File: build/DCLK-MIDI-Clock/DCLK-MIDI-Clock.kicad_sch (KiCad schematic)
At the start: 24 parts, among them J1 MIDI OUT, J2 Jack-DC, J3 MIDI OUT, SW1 CH1, SW2 CH2, SW3 SETTINGS, SW4 RotaryEncoder_Switch_MP

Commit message: pcb rev2
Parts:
- removed F1: 1A_15V, Fuse:Fuse_1812_4532Metric, symbol PCM_4ms_Regulator:Polyfuse_3A_15V
- removed SW1: CH1, Button_Switch_Keyboard:SW_Cherry_MX_1.00u_PCB, symbol Switch:SW_SPST
- removed SW2: CH2, Button_Switch_Keyboard:SW_Cherry_MX_1.00u_PCB, symbol Switch:SW_SPST
- removed SW3: SETTINGS, Button_Switch_Keyboard:SW_Cherry_MX_1.00u_PCB, symbol Switch:SW_SPST
- added C7, C8, C9: 10nF, Capacitor_SMD:C_1206_3216Metric_Pad1.33x1.80mm_HandSolder, symbol Device:C
- added J4: MIDI OUT, audioConnectors_Edit:Jack_3.5mm_CUI_SJ1-3525N_Horizontal_edit, symbol Connector_Audio:AudioJack3
- added J5: Conn_02x04_Odd_Even, Connector_PinSocket_2.54mm:PinSocket_2x04_P2.54mm_Vertical, symbol Connector_Generic:Conn_02x04_Odd_Even
- added J6: Conn_02x04_Odd_Even, Connector_PinHeader_2.54mm:PinHeader_2x04_P2.54mm_Vertical_SMD, symbol Connector_Generic:Conn_02x04_Odd_Even
- added R10: 10k, PCM_4ms_Resistor:R_0603, symbol PCM_4ms_Resistor:10k_0402
- added R5, R6: 4k7, PCM_4ms_Resistor:R_0603, symbol PCM_4ms_Resistor:10k_0402
- added R7, R8, R9: 330R, PCM_4ms_Resistor:R_0603, symbol PCM_4ms_Resistor:10k_0402
- added U2: CAP1206-x-SL, Package_SO:SOIC-14_3.9x8.7mm_P1.27mm, symbol Sensor_Touch:CAP1206-x-SL
- SSD1306: footprint SSD1306_footprint:SSD1306_OLED_Module -> SSD1306:SSD1306-128x32
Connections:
- net 3V3: now also C9.2, R10.2, R5.1, R6.1, U2.7 (VDD)
- net A: now also U1.12 (PB4/SCL2), C7.1
- net B: now also U1.13 (PB5), C8.1
- net CH1: now also J5.1 (Pin_1), J5.2 (Pin_2), J6.1 (Pin_1), J6.2 (Pin_2), U2.2 (CS1); no longer U1.34 (PB0/ADC8)
- net CH2: now also J5.3 (Pin_3), J5.4 (Pin_4), J6.3 (Pin_3), J6.4 (Pin_4), U2.13 (CS2); no longer U1.35 (PB1/ADC9)
- net ENCODER: now also U1.2 (PB13/SCK4)
- net GND: now also C7.2, C8.2, C9.1, U2.10 (CS5), U2.11 (CS4), U2.8 (GND), U2.9 (CS6)
- net LED_BEAT: now also R9.1; no longer D4.2
- net LED_CH1: now also R7.1; no longer D2.2
- net LED_CH2: now also R8.1; no longer D3.2
- net SCL0: now also R5.2, U2.5 (SMCLK)
- net SDA0: now also R6.2, U2.4 (SMDATA)
- net SETTINGS: now also J5.5 (Pin_5), J5.6 (Pin_6), J6.5 (Pin_5), J6.6 (Pin_6), U2.12 (CS3)
- net TX0: now also U1.6 (PA9/TX1); no longer U1.28 (PA2/ADC2/TX2)
- net TX1: now also U1.28 (PA2/ADC2/TX2); no longer U1.6 (PA9/TX1)
- net ISR: now reaches U1.1 (PB12/SCK3)
- net ISR: now also R10.1, U2.3 (ALERT#)
- net at C1.2, C2.1, D1.2 (A): now also J2.1
- new net: D3.2, R8.2
- new net: D4.2, R9.2
- new net: D2.2, R7.2
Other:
- note added: "5V ONLY DC Input"
- note added: "ENCODER"
- note added: "SYNC IN"
- note added: "TOUCH BUTTONS"
- note removed: "5V DC Input"
- note removed: "BUTTONS & ENCODER"
- moved on the sheet: C1, C2, C6, D1, D2, D3, D4, SSD1306, SW4

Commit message: pcb rev2
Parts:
- removed J4: MIDI OUT, audioConnectors_Edit:Jack_3.5mm_CUI_SJ1-3525N_Horizontal_edit, symbol Connector_Audio:AudioJack3
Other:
- note removed: "SYNC IN"
- moved on the sheet: J5, J6
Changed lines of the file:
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@@
 	)
 	(rectangle
-		(start 13.97 125.73)
-		(end 57.15 163.83)
-		(stroke
-			(width 0)
-			(type default)
-		)
-		(fill
-			(type none)
-		)
-	)
-	(rectangle
 		(start 102.87 86.36)
 		(end 146.05 124.46)
@@
 		)
 	)
-	(text "SYNC IN"
-		(exclude_from_sim no)
-		(at 14.732 127.762 0)
-		(effects
-			(font
-				(face "Alagard")
-				(size 2.54 2.54)
-			)
-			(justify left)
-		)
-	)
 	(text "MIDI CH2\n"
 		(exclude_from_sim no)
@@
 	(global_label "SETTINGS"
 		(shape input)
-		(at 67.31 151.13 270)
+		(at 24.13 149.86 270)
 		(fields_autoplaced yes)
 		(effects
@@
 		)
 		(property "Intersheetrefs" "${INTERSHEET_REFS}"
-			(at 67.31 162.8237 90)
+			(at 24.13 161.5537 90)
 			(effects
 				(font
@@
 	(global_label "SETTINGS"
 		(shape input)
-		(at 83.82 151.13 270)
+		(at 40.64 149.86 270)
 		(fields_autoplaced yes)
 		(effects
@@
 		)
 		(property "Intersheetrefs" "${INTERSHEET_REFS}"
-			(at 83.82 162.8237 90)
+			(at 40.64 161.5537 90)
 			(effects
 				(font
@@
 	(global_label "CH2"
 		(shape input)
-		(at 81.28 138.43 90)
+		(at 38.1 137.16 90)
 		(fields_autoplaced yes)
 		(effects
@@
 		)
 		(property "Intersheetrefs" "${INTERSHEET_REFS}"
-			(at 81.28 131.6348 90)
+			(at 38.1 130.3648 90)
 			(effects
 				(font
@@
 	(global_label "CH2"
 		(shape input)
-		(at 64.77 151.13 270)
+		(at 21.59 149.86 270)
 		(fields_autoplaced yes)
 		(effects
@@
 		)
 		(property "Intersheetrefs" "${INTERSHEET_REFS}"
-			(at 64.77 157.9252 90)
+			(at 21.59 156.6552 90)
 			(effects
 				(font
@@
 	(global_label "CH2"
 		(shape input)
-		(at 81.28 151.13 270)
+		(at 38.1 149.86 270)
 		(fields_autoplaced yes)
 		(effects
@@
 		)
 		(property "Intersheetrefs" "${INTERSHEET_REFS}"
-			(at 81.28 157.9252 90)
+			(at 38.1 156.6552 90)
 			(effects
 				(font
@@
 	(global_label "CH1"
 		(shape input)
-		(at 62.23 151.13 270)
+		(at 19.05 149.86 270)
 		(fields_autoplaced yes)
 		(effects
@@
 		)
 		(property "Intersheetrefs" "${INTERSHEET_REFS}"
-			(at 62.23 157.9252 90)
+			(at 19.05 156.6552 90)
 			(effects
 				(font
@@
 	(global_label "SETTINGS"
 		(shape input)
-		(at 67.31 138.43 90)
+		(at 24.13 137.16 90)
 		(fields_autoplaced yes)
 		(effects
@@
 		)
 		(property "Intersheetrefs" "${INTERSHEET_REFS}"
-			(at 67.31 126.7363 90)
+			(at 24.13 125.4663 90)
 			(effects
 				(font
@@
 	(global_label "CH1"
 		(shape input)
-		(at 78.74 138.43 90)
+		(at 35.56 137.16 90)
 		(fields_autoplaced yes)
 		(effects
@@
 		)
 		(property "Intersheetrefs" "${INTERSHEET_REFS}"
-			(at 78.74 131.6348 90)
+			(at 35.56 130.3648 90)
 			(effects
 				(font
@@
 	(global_label "CH1"
 		(shape input)
-		(at 62.23 138.43 90)
+		(at 19.05 137.16 90)
 		(fields_autoplaced yes)
 		(effects
@@
 		)
 		(property "Intersheetrefs" "${INTERSHEET_REFS}"
-			(at 62.23 131.6348 90)
+			(at 19.05 130.3648 90)
 			(effects
 				(font
@@
 	(global_label "CH1"
 		(shape input)
-		(at 78.74 151.13 270)
+		(at 35.56 149.86 270)
 		(fields_autoplaced yes)
 		(effects
@@
 		)
 		(property "Intersheetrefs" "${INTERSHEET_REFS}"
-			(at 78.74 157.9252 90)
+			(at 35.56 156.6552 90)
 			(effects
 				(font
@@
 	(global_label "SETTINGS"
 		(shape input)
-		(at 83.82 138.43 90)
+		(at 40.64 137.16 90)
 		(fields_autoplaced yes)
 		(effects
@@
 		)
 		(property "Intersheetrefs" "${INTERSHEET_REFS}"
-			(at 83.82 126.7363 90)
+			(at 40.64 125.4663 90)
 			(effects
 				(font
@@
 	(global_label "CH2"
 		(shape input)
-		(at 64.77 138.43 90)
+		(at 21.59 137.16 90)
 		(fields_autoplaced yes)
 		(effects
@@
 		)
 		(property "Intersheetrefs" "${INTERSHEET_REFS}"
-			(at 64.77 131.6348 90)
+			(at 21.59 130.3648 90)
 			(effects
 				(font
@@
 	(symbol
 		(lib_id "Connector_Generic:Conn_02x04_Odd_Even")
-		(at 64.77 146.05 90)
+		(at 21.59 144.78 90)
 		(unit 1)
 		(exclude_from_sim no)
@@
 		(fields_autoplaced yes)
 		(property "Reference" "J5"
-			(at 72.39 143.5099 90)
+			(at 29.21 142.2399 90)
 			(effects
 				(font
@@
 		)
 		(property "Value" "Conn_02x04_Odd_Even"
-			(at 72.39 146.0499 90)
+			(at 29.21 144.7799 90)
 			(effects
 				(font
@@
 		)
 		(property "Footprint" "Connector_PinSocket_2.54mm:PinSocket_2x04_P2.54mm_Vertical"
-			(at 64.77 146.05 0)
+			(at 21.59 144.78 0)
 			(effects
 				(font
@@
 		)
 		(property "Datasheet" "~"
-			(at 64.77 146.05 0)
+			(at 21.59 144.78 0)
 			(effects
 				(font
@@
 		)
 		(property "Description" "Generic connector, double row, 02x04, odd/even pin numbering scheme (row 1 odd numbers, row 2 even numbers), script generated (kicad-library-utils/schlib/autogen/connector/)"
-			(at 64.77 146.05 0)
+			(at 21.59 144.78 0)
 			(effects
 				(font
@@
 	)
 	(symbol
-		(lib_id "Connector_Audio:AudioJack3")
-		(at 21.59 139.7 0)
-		(unit 1)
-		(exclude_from_sim no)
-		(in_bom yes)
-		(on_board yes)
-		(dnp no)
-		(fields_autoplaced yes)
-		(property "Reference" "J4"
-			(at 19.685 130.81 0)
-			(effects
-				(font
-					(size 1.27 1.27)
-				)
-			)
-		)
-		(property "Value" "MIDI OUT"
-			(at 19.685 133.35 0)
-			(effects
-				(font
-					(size 1.27 1.27)
-				)
-			)
-		)
-		(property "Footprint" "audioConnectors_Edit:Jack_3.5mm_CUI_SJ1-3525N_Horizontal_edit"
-			(at 21.59 139.7 0)
-			(effects
-				(font
-					(size 1.27 1.27)
-				)
-				(hide yes)
-			)
-		)
-		(property "Datasheet" "~"
-			(at 21.59 139.7 0)
-			(effects
-				(font
-					(size 1.27 1.27)
-				)
-				(hide yes)
-			)
-		)
-		(property "Description" "Audio Jack, 3 Poles (Stereo / TRS)"
-			(at 21.59 139.7 0)
-			(effects
-				(font
-					(size 1.27 1.27)
-				)
-				(hide yes)
-			)
-		)
-		(pin "S"
-		)
-		(pin "T"
-		)
-		(pin "R"
-		)
-		(instances
-			(project "DCLK-MIDI-Clock"
-				(path "/42d00d8e-48e3-47e6-b456-ac5bd2d9bc78"
-					(reference "J4")
-					(unit 1)
-				)
-			)
-		)
-	)
-	(symbol
 		(lib_id "power:GND")
 		(at 190.5 35.56 0)
@@
 	(symbol
 		(lib_id "Connector_Generic:Conn_02x04_Odd_Even")
-		(at 81.28 146.05 90)
+		(at 38.1 144.78 90)
 		(unit 1)
 		(exclude_from_sim no)
@@
 		(fields_autoplaced yes)
 		(property "Reference" "J6"
-			(at 88.9 143.5099 90)
+			(at 45.72 142.2399 90)
 			(effects
 				(font
@@
 		)
 		(property "Value" "Conn_02x04_Odd_Even"
-			(at 88.9 146.0499 90)
+			(at 45.72 144.7799 90)
 			(effects
 				(font
@@
 		)
 		(property "Footprint" "Connector_PinHeader_2.54mm:PinHeader_2x04_P2.54mm_Vertical_SMD"
-			(at 81.28 146.05 0)
+			(at 38.1 144.78 0)
 			(effects
 				(font
@@
 		)
 		(property "Datasheet" "~"
-			(at 81.28 146.05 0)
+			(at 38.1 144.78 0)
 			(effects
 				(font
@@
 		)
 		(property "Description" "Generic connector, double row, 02x04, odd/even pin numbering scheme (row 1 odd numbers, row 2 even numbers), script generated (kicad-library-utils/schlib/autogen/connector/)"
-			(at 81.28 146.05 0)
+			(at 38.1 144.78 0)
 			(effects
 				(font

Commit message: SYNC OUT
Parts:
- added C10: 100nF, Capacitor_SMD:C_0603_1608Metric, symbol PCM_4ms_Capacitor:100nF_0603_16V
- added J7: SYNC 1 OUT, audioConnectors_Edit:Jack_3.5mm_CUI_SJ1-3525N_Horizontal_edit, symbol Connector_Audio:AudioJack3
- added J8: SYNC 2 OUT, audioConnectors_Edit:Jack_3.5mm_CUI_SJ1-3525N_Horizontal_edit, symbol Connector_Audio:AudioJack3
- added R11, R12, R13, R14: 100k, Resistor_SMD:R_0402_1005Metric, symbol PCM_4ms_Resistor:10k_0402
- added R15, R16, R17, R18: 1k, Resistor_SMD:R_0402_1005Metric, symbol PCM_4ms_Resistor:10k_0402
- added U3: 74AHCT125, Package_SO:SOIC-14_3.9x8.7mm_P1.27mm, symbol DCLK:74AHCT125
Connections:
- net GND: now also C10.2, J7.S, J8.S, R11.2, R12.2, R13.2, R14.2, U3.1 (~{1OE}), U3.10 (~{3OE}), U3.13 (~{4OE}), U3.4 (~{2OE}), U3.7 (GND)
- net Vcc: now also C10.1, U3.14 (VCC)
- net RUN2: now reaches U1.30 (PA4/ADC4)
- net RUN2: now also R14.1, U3.12 (4A)
- net SYNC2: now reaches U1.31 (PA5/ADC5/SCK1)
- net SYNC2: now also R13.1, U3.9 (3A)
- net RUN1: now reaches U1.4 (PB15/MOSI2)
- net RUN1: now also R12.1, U3.5 (2A)
- net SYNC1: now reaches U1.5 (PA8)
- net SYNC1: now also R11.1, U3.2 (1A)
- new net: R18.1, U3.11 (4Y)
- new net: R15.1, U3.3 (1Y)
- new net: R16.1, U3.6 (2Y)
- new net: R17.1, U3.8 (3Y)
- new net RUN1_OUT: J7.R, R16.2
- new net RUN2_OUT: J8.R, R18.2
- new net SYNC1_OUT: J7.T, R15.2
- new net SYNC2_OUT: J8.T, R17.2
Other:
- note added: "SYNC OUTS: 5V, tip = clock pulse, ring = run gate (high while channel plays) SYNC1/RUN1 follow CH1, SYNC2/RUN2 follow CH2. 1k series = short-proof for TS plugs"

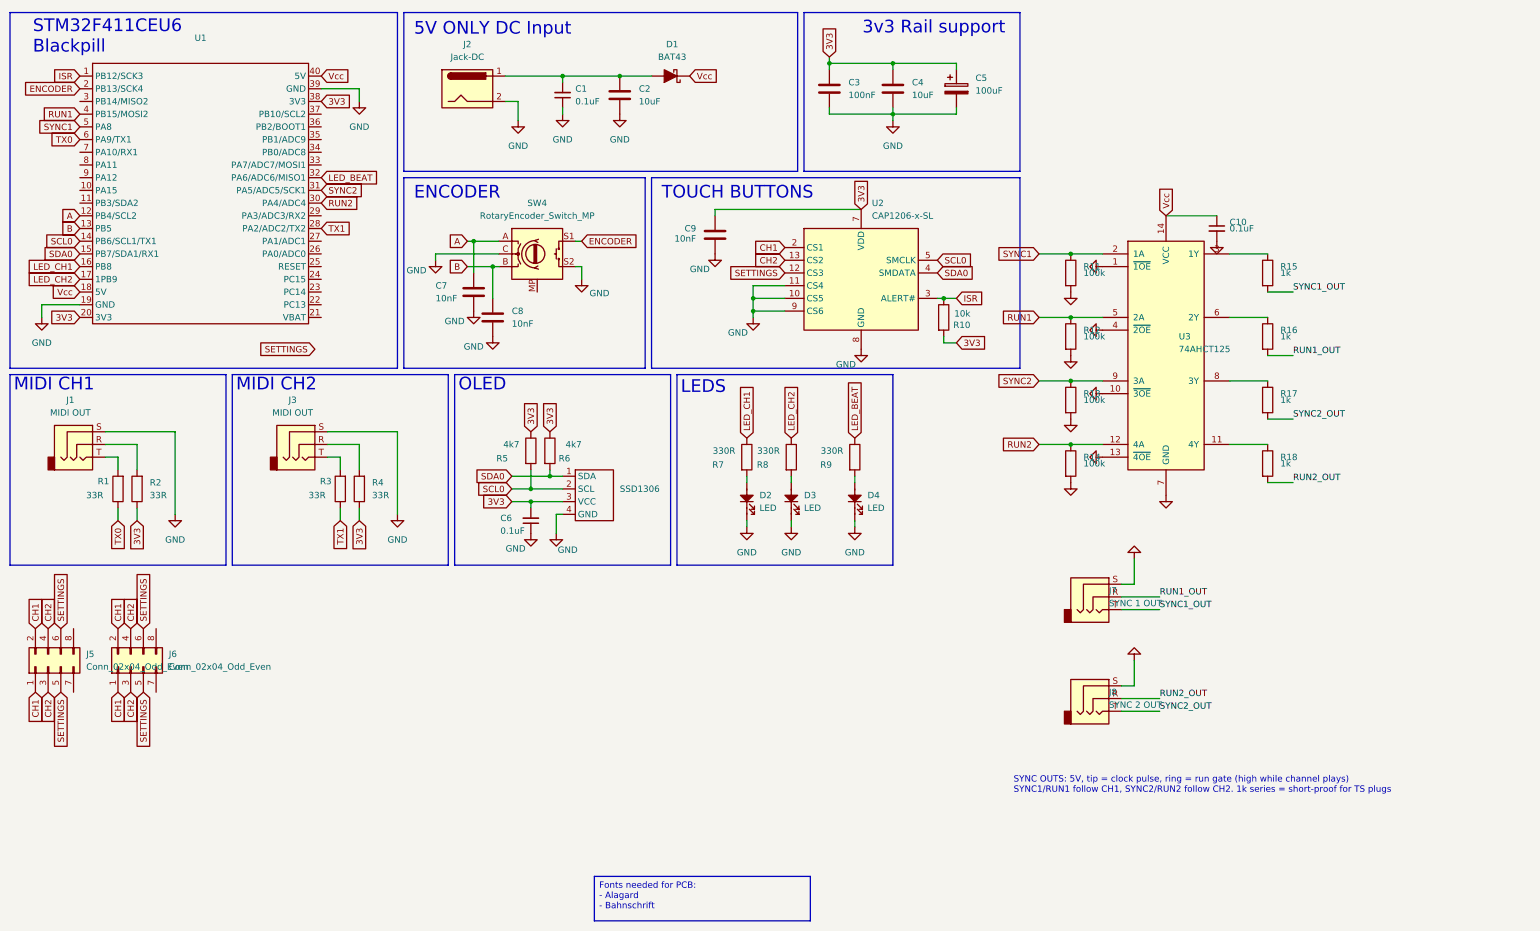
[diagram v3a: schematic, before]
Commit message: PCB update
-Added 2x Sync Output
-Moved 5V DC in
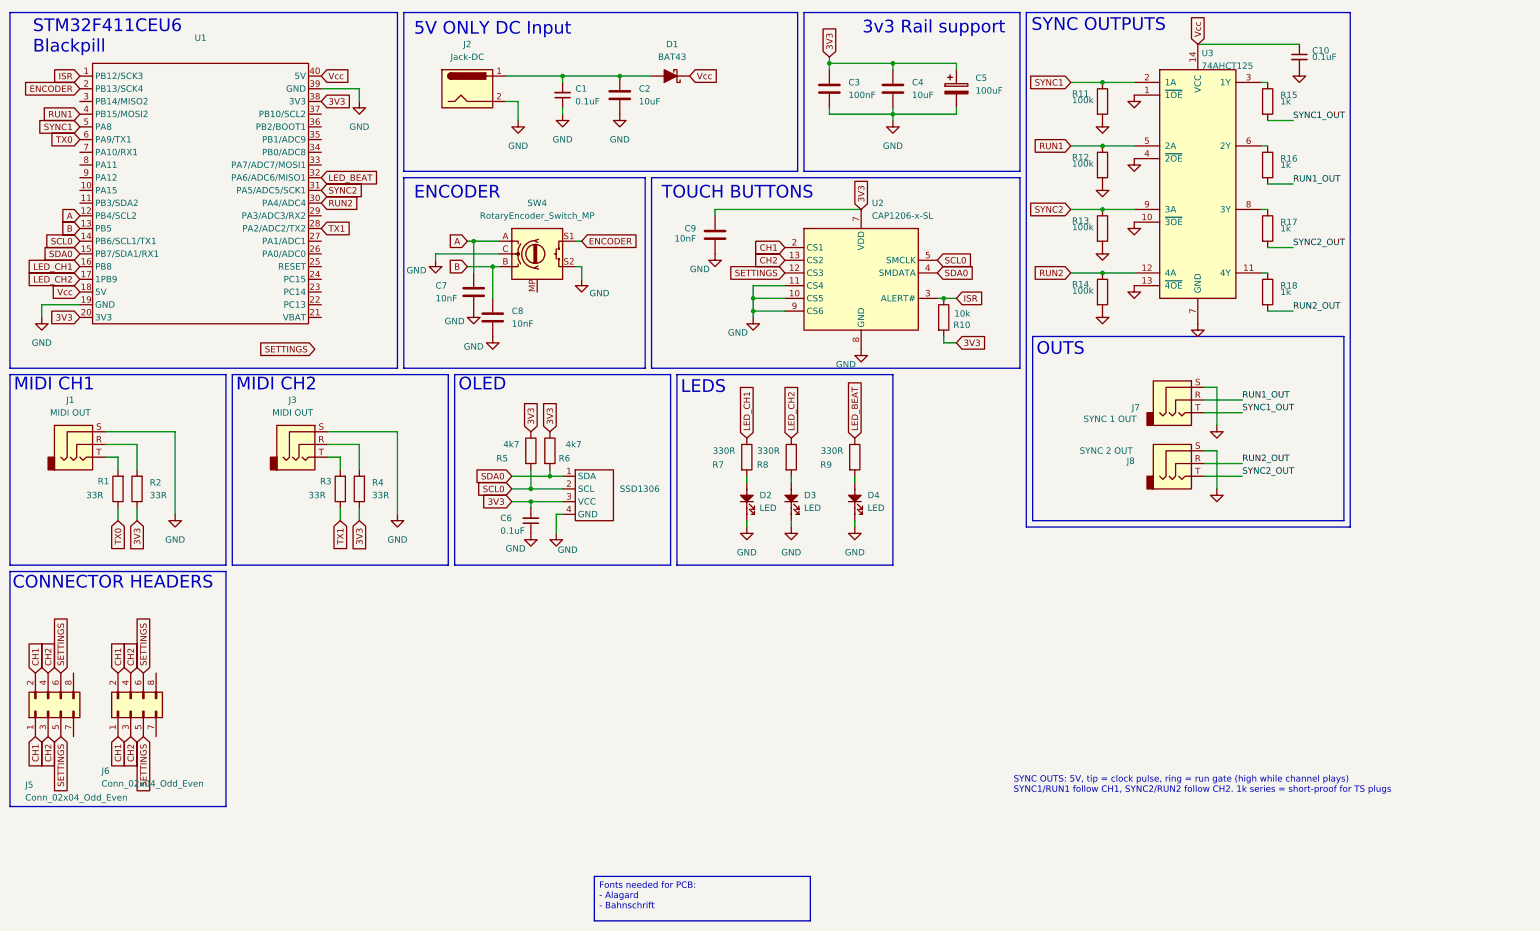
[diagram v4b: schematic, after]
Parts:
- J7, J8: footprint audioConnectors_Edit:Jack_3.5mm_CUI_SJ1-3525N_Horizontal_edit -> PJ307-TRS:PJ307-TRS-SOCKET
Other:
- note added: "CONNECTOR HEADERS"
- note added: "OUTS"
- note added: "SYNC OUTPUTS"
- moved on the sheet: C10, J5, J6, J7, J8, R11, R12, R13, R14, R15, R16, R17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

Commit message: sch and pcb tweaks
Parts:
- R1, R2, R3, R4: value 220R -> 33R
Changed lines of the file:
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@@
 			)
 		)
-		(property "Value" "220R"
+		(property "Value" "33R"
 			(at 82.55 109.22 90)
 			(effects
@@
 			)
 		)
-		(property "Value" "220R"
+		(property "Value" "33R"
 			(at 38.1 109.22 90)
 			(effects
@@
 			)
 		)
-		(property "Value" "220R"
+		(property "Value" "33R"
 			(at 86.36 109.22 90)
 			(effects
@@
 			)
 		)
-		(property "Value" "220R"
+		(property "Value" "33R"
 			(at 41.91 109.22 90)
 			(effects

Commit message: pcb update
-fixed oled positions
- fixed resistor inconsistencies
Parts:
- R1, R2, R3, R4: Specifications 10k, 1%, 1/10W, 0402 -> 33R, 1%, 1/16W, 0603
- R5, R6: Specifications 10k, 1%, 1/10W, 0402 -> 4k7, 1%, 1/16W, 0603
- R7, R8, R9: Specifications 10k, 1%, 1/10W, 0402 -> 330R, 1%, 1/16W, 0603
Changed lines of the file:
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@@
 			)
 		)
-		(property "Description" "10k, 1%, 1/16W, 0603"
+		(property "Description" "33R, 1%, 1/16W, 0603"
 			(at 80.01 109.22 0)
 			(effects
@@
 			)
 		)
-		(property "Specifications" "10k, 1%, 1/10W, 0402"
+		(property "Specifications" "33R, 1%, 1/16W, 0603"
 			(at 82.55 101.346 0)
 			(effects
@@
 			)
 		)
-		(property "Description" "10k, 1%, 1/16W, 0603"
+		(property "Description" "330R, 1%, 1/16W, 0603"
 			(at 170.18 102.87 0)
 			(effects
@@
 			)
 		)
-		(property "Specifications" "10k, 1%, 1/10W, 0402"
+		(property "Specifications" "330R, 1%, 1/16W, 0603"
 			(at 167.64 110.744 0)
 			(effects
@@
 			)
 		)
-		(property "Description" "10k, 1%, 1/16W, 0603"
+		(property "Description" "4k7, 1%, 1/16W, 0603"
 			(at 121.92 101.6 0)
 			(effects
@@
 			)
 		)
-		(property "Specifications" "10k, 1%, 1/10W, 0402"
+		(property "Specifications" "4k7, 1%, 1/16W, 0603"
 			(at 119.38 109.474 0)
 			(effects
@@
 			)
 		)
-		(property "Description" "10k, 1%, 1/16W, 0603"
+		(property "Description" "33R, 1%, 1/16W, 0603"
 			(at 35.56 109.22 0)
 			(effects
@@
 			)
 		)
-		(property "Specifications" "10k, 1%, 1/10W, 0402"
+		(property "Specifications" "33R, 1%, 1/16W, 0603"
 			(at 38.1 101.346 0)
 			(effects
@@
 			)
 		)
-		(property "Description" "10k, 1%, 1/16W, 0603"
+		(property "Description" "4k7, 1%, 1/16W, 0603"
 			(at 118.11 101.6 0)
 			(effects
@@
 			)
 		)
-		(property "Specifications" "10k, 1%, 1/10W, 0402"
+		(property "Specifications" "4k7, 1%, 1/16W, 0603"
 			(at 115.57 109.474 0)
 			(effects
@@
 			)
 		)
-		(property "Description" "10k, 1%, 1/16W, 0603"
+		(property "Description" "330R, 1%, 1/16W, 0603"
 			(at 182.88 102.87 0)
 			(effects
@@
 			)
 		)
-		(property "Specifications" "10k, 1%, 1/10W, 0402"
+		(property "Specifications" "330R, 1%, 1/16W, 0603"
 			(at 180.34 110.744 0)
 			(effects
@@
 			)
 		)
-		(property "Description" "10k, 1%, 1/16W, 0603"
+		(property "Description" "33R, 1%, 1/16W, 0603"
 			(at 83.82 109.22 0)
 			(effects
@@
 			)
 		)
-		(property "Specifications" "10k, 1%, 1/10W, 0402"
+		(property "Specifications" "33R, 1%, 1/16W, 0603"
 			(at 86.36 101.346 0)
 			(effects
@@
 			)
 		)
-		(property "Description" "10k, 1%, 1/16W, 0603"
+		(property "Description" "33R, 1%, 1/16W, 0603"
 			(at 39.37 109.22 0)
 			(effects
@@
 			)
 		)
-		(property "Specifications" "10k, 1%, 1/10W, 0402"
+		(property "Specifications" "33R, 1%, 1/16W, 0603"
 			(at 41.91 101.346 0)
 			(effects
@@
 			)
 		)
-		(property "Description" "10k, 1%, 1/16W, 0603"
+		(property "Description" "330R, 1%, 1/16W, 0603"
 			(at 161.29 102.87 0)
 			(effects
@@
 			)
 		)
-		(property "Specifications" "10k, 1%, 1/10W, 0402"
+		(property "Specifications" "330R, 1%, 1/16W, 0603"
 			(at 158.75 110.744 0)
 			(effects

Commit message: updated bom
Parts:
- C1, C6: value 100nF_0603_16V -> 100nF
- C10: footprint Capacitor_SMD:C_0603_1608Metric -> Capacitor_SMD:C_1206_3216Metric
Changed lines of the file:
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@@
 			)
 		)
-		(property "Value" "100nF_0603_16V"
+		(property "Value" "100nF"
 			(at 118.11 119.38 0)
 			(effects
@@
 			)
 		)
-		(property "Value" "100nF_0603_16V"
+		(property "Value" "100nF"
 			(at 124.46 34.29 0)
 			(effects
@@
 			)
 		)
-		(property "Footprint" "Capacitor_SMD:C_0603_1608Metric"
+		(property "Footprint" "Capacitor_SMD:C_1206_3216Metric"
 			(at 271.78 22.86 0)
 			(effects
